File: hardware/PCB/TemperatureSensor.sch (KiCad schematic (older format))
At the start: 0 parts

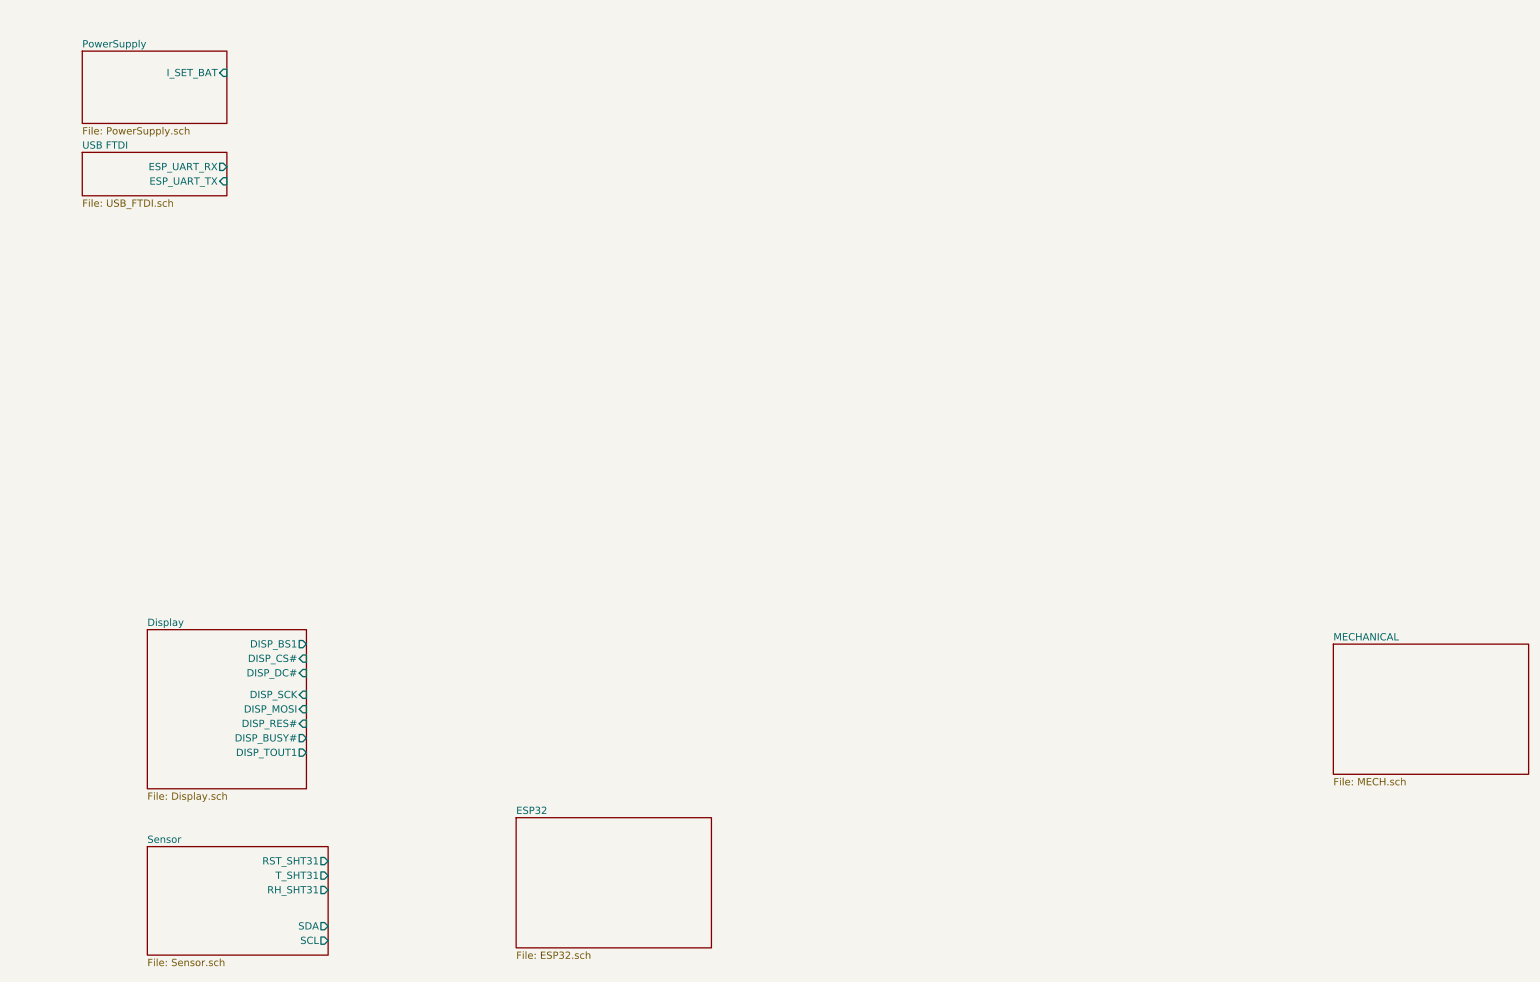
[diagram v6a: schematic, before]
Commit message: changed FTDI chip to full handshake chip
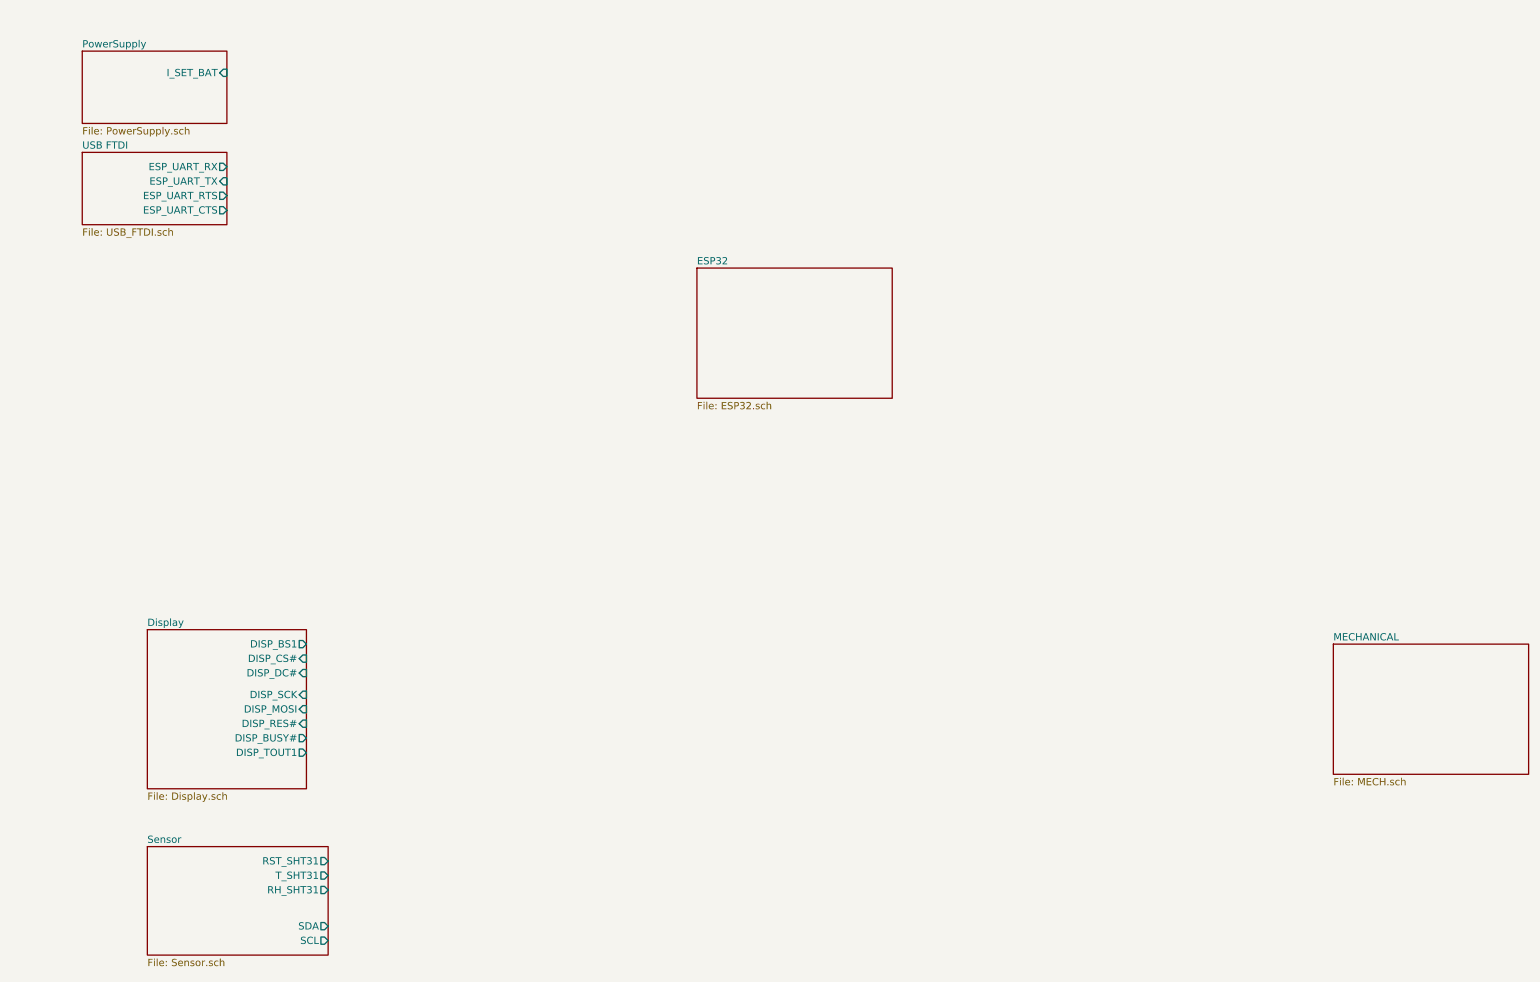
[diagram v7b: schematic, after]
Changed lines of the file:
@@
 $EndSheet
 $Sheet
-S 4000 6300 1350 900
+S 5250 2500 1350 900
 U 5FCFD0E2
 F0 "ESP32" 50
@@
 $EndSheet
 $Sheet
-S 1000 1700 1000 300
+S 1000 1700 1000 500
 U 5FE9624E
 F0 "USB FTDI" 50
@@
 F2 "ESP_UART_RX" O R 2000 1800 50
 F3 "ESP_UART_TX" I R 2000 1900 50
+F4 "ESP_UART_RTS" O R 2000 2000 50
+F5 "ESP_UART_CTS" O R 2000 2100 50
 $EndSheet
 $EndSCHEMATC

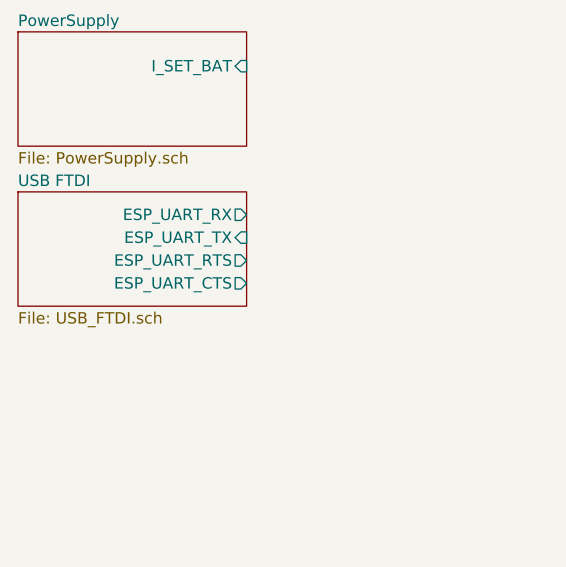
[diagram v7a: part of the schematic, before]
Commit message: add ESP32 bootloader circuit
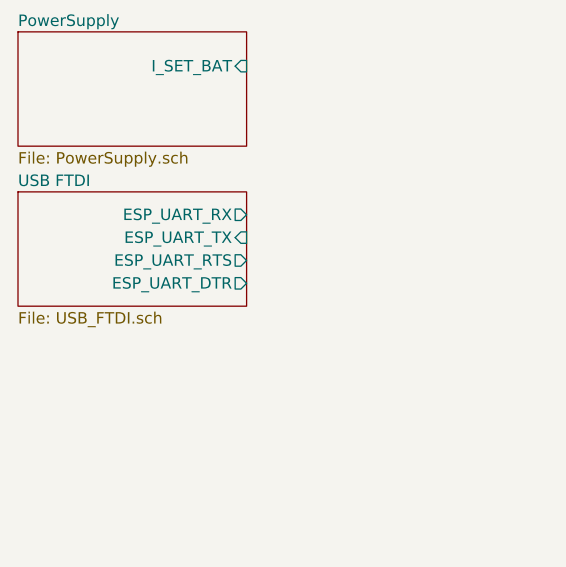
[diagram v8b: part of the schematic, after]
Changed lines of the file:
@@
 F3 "ESP_UART_TX" I R 2000 1900 50
 F4 "ESP_UART_RTS" O R 2000 2000 50
-F5 "ESP_UART_CTS" O R 2000 2100 50
+F5 "ESP_UART_DTR" O R 2000 2100 50
 $EndSheet
 $EndSCHEMATC
